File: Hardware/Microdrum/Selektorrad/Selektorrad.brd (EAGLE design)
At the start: 63.8 x 33 mm, 11 parts, among them IC1 74AC138N

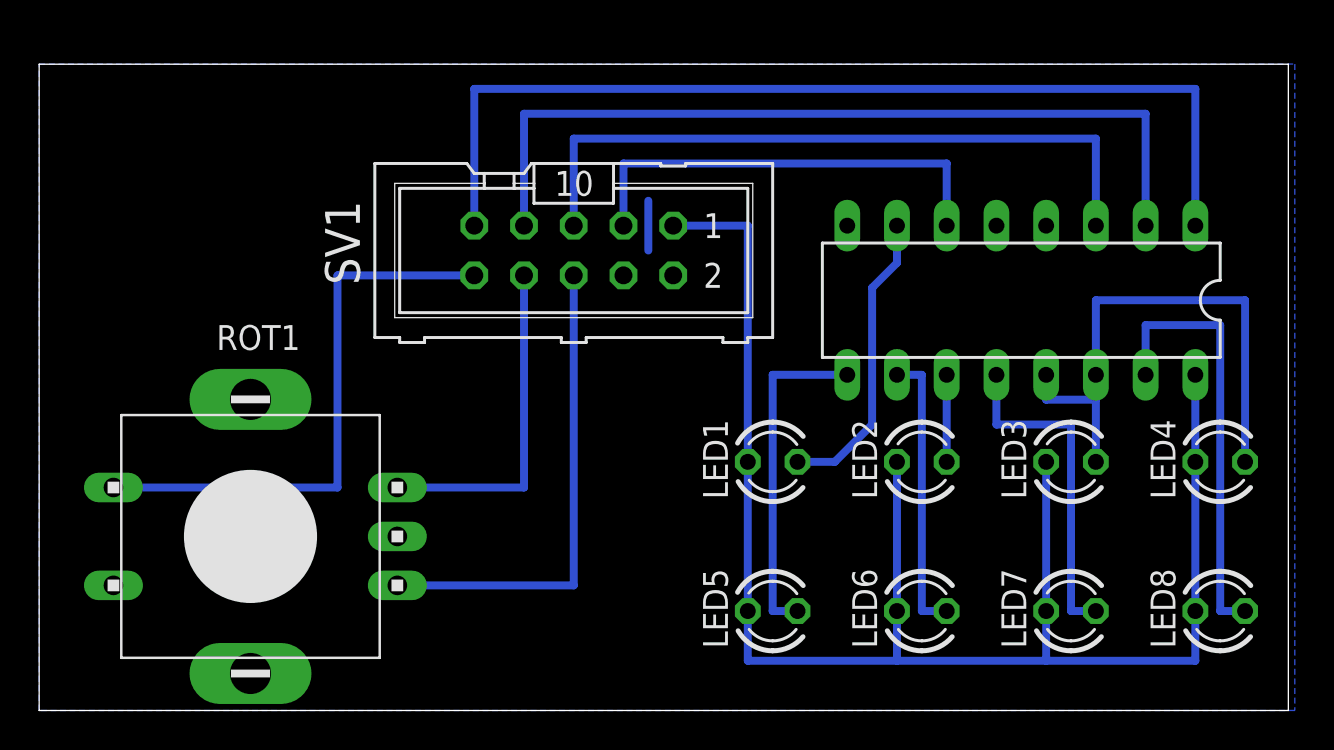
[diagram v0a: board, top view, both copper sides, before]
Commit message: minimized selector board
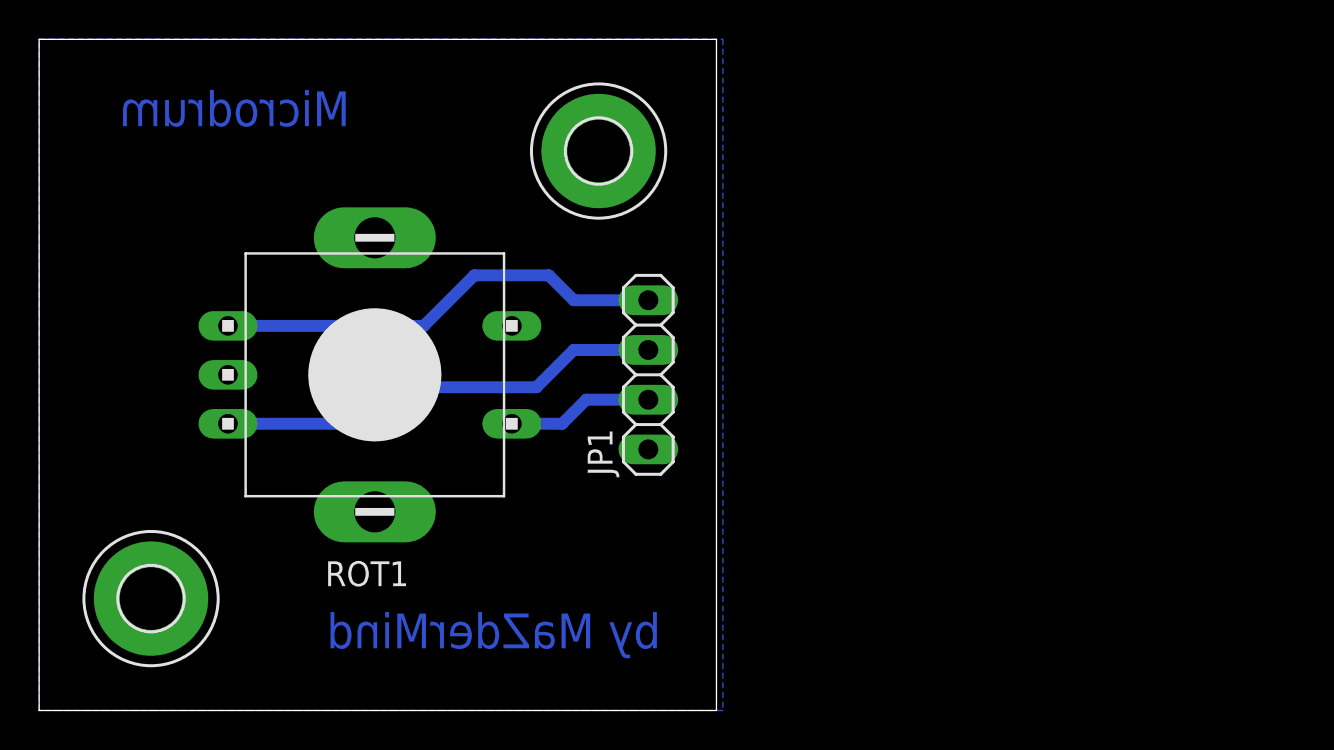
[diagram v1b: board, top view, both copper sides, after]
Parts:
- removed IC1: 74AC138N, 74xx-eu:DIL16
- removed LED1, LED2, LED3, LED4, LED5, LED6, LED7, LED8: (no value), led:LED3MM
- removed SV1: (no value), con-harting-ml:ML10
- added H2, H3: MOUNT-PAD-ROUND3.2, holes:3,2-PAD
- added JP1: (no value), pinhead:1X04
- moved ROT1 10.4 mm to (17.1, 17.1), turned to 270 degrees
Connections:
- removed net N$10: IC1.1, SV1.9
- removed net N$11: IC1.2, SV1.7
- removed net N$12: IC1.3, SV1.5
- removed net N$13: IC1.6, SV1.3
- removed net N$14: ROT1.B, SV1.8
- removed net N$2: IC1.9, LED5.K
- removed net N$3: IC1.10, LED6.K
- removed net N$4: IC1.11, LED2.K
- removed net N$5: IC1.12, LED7.K
- removed net N$7: IC1.13, LED3.K
- removed net N$8: IC1.15, LED8.K
- removed net N$9: IC1.14, LED4.K
- removed net VCC: IC1.16, LED1.A, LED2.A, LED3.A, LED4.A, LED5.A, LED6.A, LED7.A, LED8.A, SV1.1
- net GND: now also JP1.1; no longer IC1.4, IC1.5, IC1.8, SV1.2
- net N$1: now also JP1.3, ROT1.B; no longer IC1.7, LED1.K
- net N$15: now also JP1.2; no longer SV1.10
- net N$6: now also JP1.4; no longer SV1.6
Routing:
- net VCC: track 83.8 -> 0.00 mm
- net N$10: track 50.8 -> 0.00 mm
- net N$11: track 43.2 -> 0.00 mm
- net N$12: track 35.6 -> 0.00 mm
- net N$13: track 22.9 -> 0.00 mm
- net N$8: track 22.2 -> 0.00 mm
- net N$15: track 29.3 -> 7.52 mm
- net N$9: track 19.7 -> 0.00 mm
- net N$14: track 17.3 -> 0.00 mm
- net N$5: track 17.1 -> 0.00 mm
- net N$2: track 17.1 -> 0.00 mm
- net N$3: track 14.6 -> 0.00 mm
- net N$1: track 15.3 -> 23.1 mm
- net N$7: track 6.98 -> 0.00 mm
- net N$4: track 4.45 -> 0.00 mm
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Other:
- board size 63.8 x 33 mm -> 34.6 x 34.3 mm
- board text added: "Microdrum"
- board text added: "by MaZderMind"
